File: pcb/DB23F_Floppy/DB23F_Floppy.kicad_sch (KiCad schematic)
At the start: 3 parts, among them J1 DB23F SOLDER CUPS, J2 MOTHERBOARD PINS, J3 MANUAL SHIELD STRAPS

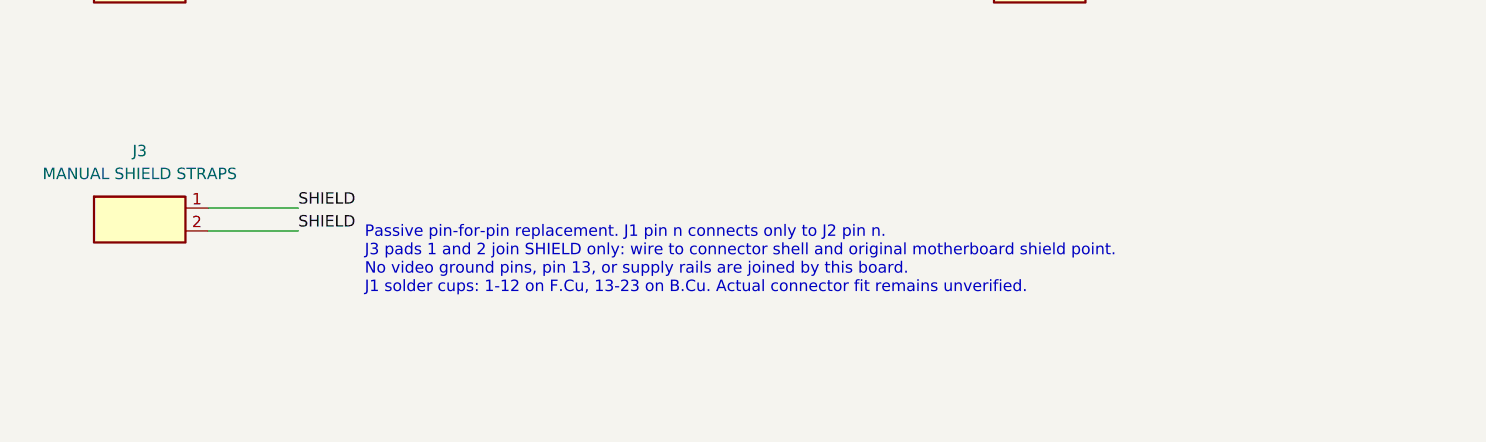
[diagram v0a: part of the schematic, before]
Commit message: Add bolted DB23 base and clip-on cap for revision 0.5
Shorten both adapter PCBs to Y13, add mounting ears at the original shell anchors, and separate the shell-wire pads from the nut-bearing lands. Preserve all 23 independent signal circuits.

Replace recessed top screw heads with upward M3 mounting screws, a solid printed base with integrated feet, and a keyed black cap. Add clip-fit coupons, updated loading jig, reference-driven corner reliefs and an insulated underside screw-head stack with deliberate shell-ground wiring.

Regenerate native KiCad projects, fit-prototype manufacturing files, printable STL/STEP, previews, five-page drawings, BOM, assembly guide and AI handover. Both native PCB DRC reports are clean; 648 electrical, 176 mechanical and 68 reference/alignment checks pass within their recorded scope. Physical fit, printed strength and Amiga operation remain untested.
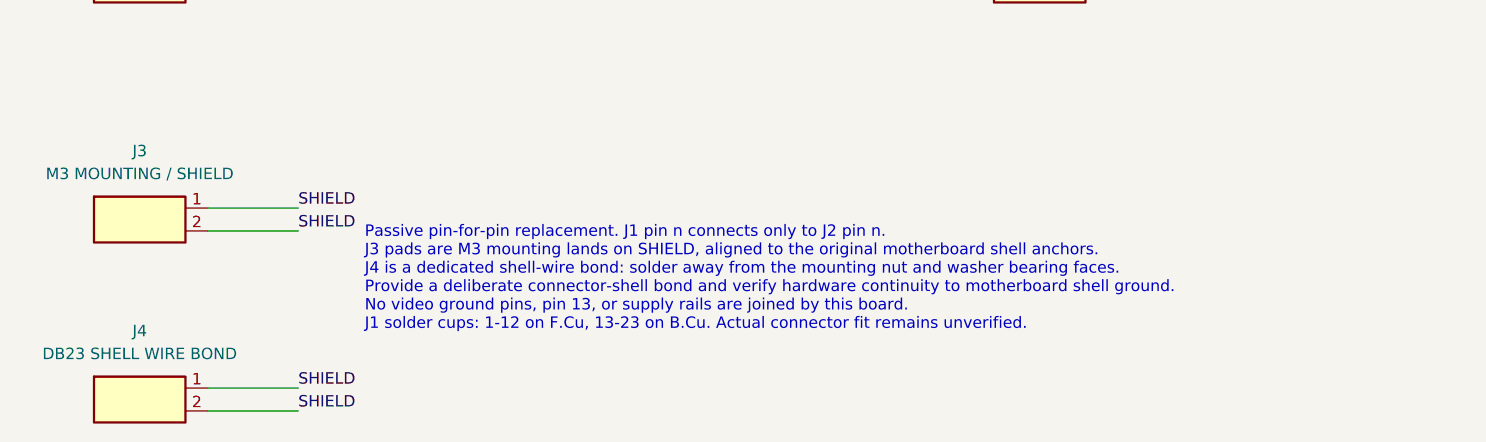
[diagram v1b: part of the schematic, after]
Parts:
- added J4: DB23 SHELL WIRE BOND, DB23_Local:ShellBond_F, symbol DB23_Local:ShellBond
- J3: value MANUAL SHIELD STRAPS -> M3 MOUNTING / SHIELD; footprint DB23_Local:ShieldStraps_F -> DB23_Local:MountingShield_F; symbol DB23_Local:ShieldStraps -> DB23_Local:MountingShield
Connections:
- net SHIELD: now also J4.1, J4.2
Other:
- note added: "Passive pin-for-pin replacement. J1 pin n connects only to J2 pin n. J3 pads are M3 mounting lands on SHIELD, aligned to the original motherboard shell anchors. J4 is a dedicated shell-wire bond: solder away from the mounting nut and washer bearing faces. Provide a deliberate connector-shell bond and verify hardware continuity to motherboard shell ground. No video ground pins, pin 13, or supply r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"
- note removed: "Passive pin-for-pin replacement. J1 pin n connects only to J2 pin n. J3 pads 1 and 2 join SHIELD only: wire to connector shell and original motherboard shield point. No video ground pins, pin 13, or supply rails are joined by this board. J1 solder cups: 1-12 on F.Cu, 13-23 on B.Cu. Actual connector fit remains unverified."
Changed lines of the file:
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@@
 (kicad_sch (version 20230121) (generator eeschema)
  (paper "A4")
- (title_block (title "DB23F_Floppy DB23 replacement") (date "2026-10-29") (rev "0.3") (company "UK Computing Limited") (comment 1 "FIT PROTOTYPE - measure selected solder-cup DB23 before manufacture"))
+ (title_block (title "DB23F_Floppy DB23 replacement") (date "2026-10-29") (rev "0.5") (company "UK Computing Limited") (comment 1 "FIT PROTOTYPE - measure selected solder-cup DB23 before manufacture"))
  (symbol (lib_id "DB23_Local:Cups23") (at 60 40 0) (unit 1) (in_bom yes) (on_board yes)
  (property "Reference" "J1" (at 60 33.65 0) (effects (font (size 1.27 1.27))))
@@
  (pin "23")
  (instances (project "DB23F_Floppy" (path "/d46512ce-1690-52f3-b622-f04fb61af732" (reference "J2") (unit 1)))))
- (symbol (lib_id "DB23_Local:ShieldStraps") (at 60 120 0) (unit 1) (in_bom yes) (on_board yes)
+ (symbol (lib_id "DB23_Local:MountingShield") (at 60 120 0) (unit 1) (in_bom yes) (on_board yes)
  (property "Reference" "J3" (at 60 113.65 0) (effects (font (size 1.27 1.27))))
- (property "Value" "MANUAL SHIELD STRAPS" (at 60 116.19 0) (effects (font (size 1.27 1.27))))
- (property "Footprint" "DB23_Local:ShieldStraps_F" (at 60 120 0) (effects (font (size 1.27 1.27)) hide))
+ (property "Value" "M3 MOUNTING / SHIELD" (at 60 116.19 0) (effects (font (size 1.27 1.27))))
+ (property "Footprint" "DB23_Local:MountingShield_F" (at 60 120 0) (effects (font (size 1.27 1.27)) hide))
  (property "Datasheet" "" (at 60 120 0) (effects (font (size 1.27 1.27)) hide))
  (pin "1")
  (pin "2")
  (instances (project "DB23F_Floppy" (path "/d46512ce-1690-52f3-b622-f04fb61af732" (reference "J3") (unit 1)))))
+ (symbol (lib_id "DB23_Local:ShellBond") (at 60 140 0) (unit 1) (in_bom yes) (on_board yes)
+ (property "Reference" "J4" (at 60 133.65 0) (effects (font (size 1.27 1.27))))
+ (property "Value" "DB23 SHELL WIRE BOND" (at 60 136.19 0) (effects (font (size 1.27 1.27))))
+ (property "Footprint" "DB23_Local:ShellBond_F" (at 60 140 0) (effects (font (size 1.27 1.27)) hide))
+ (property "Datasheet" "" (at 60 140 0) (effects (font (size 1.27 1.27)) hide))
+ (pin "1")
+ (pin "2")
+ (instances (project "DB23F_Floppy" (path "/d46512ce-1690-52f3-b622-f04fb61af732" (reference "J4") (unit 1)))))
  (wire (pts (xy 67.62 40.000) (xy 152.38 40.000)) (stroke (width 0) (type default)))
  (label "P01" (at 105 40.000 0) (effects (font (size 1.27 1.27)) (justify left bottom)))
@@
  (wire (pts (xy 67.62 122.540) (xy 77.62 122.540)) (stroke (width 0) (type default)))
  (label "SHIELD" (at 77.62 122.54 0) (effects (font (size 1.27 1.27)) (justify left bottom)))
- (text "Passive pin-for-pin replacement. J1 pin n connects only to J2 pin n.\nJ3 pads 1 and 2 join SHIELD only: wire to connector shell and original motherboard shield point.\nNo video ground pins, pin 13, or supply rails are joined by this board.\nJ1 solder cups: 1-12 on F.Cu, 13-23 on B.Cu. Actual connector fit remains unverified." (at 85 122 0) (effects (font (size 1.27 1.27)) (justify left top)))
+ (wire (pts (xy 67.62 140.000) (xy 77.62 140.000)) (stroke (width 0) (type default)))
+ (label "SHIELD" (at 77.62 140.0 0) (effects (font (size 1.27 1.27)) (justify left bottom)))
+ (wire (pts (xy 67.62 142.540) (xy 77.62 142.540)) (stroke (width 0) (type default)))
+ (label "SHIELD" (at 77.62 142.54 0) (effects (font (size 1.27 1.27)) (justify left bottom)))
+ (text "Passive pin-for-pin replacement. J1 pin n connects only to J2 pin n.\nJ3 pads are M3 mounting lands on SHIELD, aligned to the original motherboard shell anchors.\nJ4 is a dedicated shell-wire bond: solder away from the mounting nut and washer bearing faces.\nProvide a deliberate connector-shell bond and verify hardware continuity to motherboard shell ground.\nNo video ground pins, pin 13, or supply rails are joined by this board.\nJ1 solder cups: 1-12 on F.Cu, 13-23 on B.Cu. Actual connector fit remains unverified." (at 85 122 0) (effects (font (size 1.27 1.27)) (justify left top)))
  (sheet_instances (path "/" (page "1")))
 )

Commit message: Refine DB23 end walls, PCB labels and project credits
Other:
- company: UK Computing Limited -> Amiga DB23
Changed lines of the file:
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@@
 (kicad_sch (version 20230121) (generator eeschema)
  (paper "A4")
- (title_block (title "DB23F_Floppy DB23 replacement") (date "2026-10-29") (rev "0.5") (company "UK Computing Limited") (comment 1 "FIT PROTOTYPE - measure selected solder-cup DB23 before manufacture"))
+ (title_block (title "DB23F_Floppy DB23 replacement") (date "2026-10-29") (rev "0.5") (company "Amiga DB23") (comment 1 "FIT PROTOTYPE - measure selected solder-cup DB23 before manufacture") (comment 2 "Paul of UK Computing Limited; Jon of JMC Electronics; AI assistance through Codex"))
  (symbol (lib_id "DB23_Local:Cups23") (at 60 40 0) (unit 1) (in_bom yes) (on_board yes)
  (property "Reference" "J1" (at 60 33.65 0) (effects (font (size 1.27 1.27))))
